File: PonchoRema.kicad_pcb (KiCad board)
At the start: 2 copper layers, 138.6 x 86.2 mm, 133 parts, among them J1 Conn_01x05, J10 Conn_01x05, J2 Conn_01x05, J3 Conn_01x05, J4 Conn_01x05, J5 Conn_01x05, J6 Conn_01x05, J7 Conn_01x03, J8 Conn_01x05, J9 Conn_01x05, P1 Conn_02x10_Odd_Even, SW1 SW_Push, SW2 SW_Push, U1 RPi-Pico, U10 ULN2004, U2 LTV-847S, U3 LTV-847S, U4 LTV-847S, U5 LTV-847S, U6 74HC14, U7 74HC14, U8 74HC14, U9 ULN2004

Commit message: Avances con el pcb antes de un laaargo finde
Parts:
- moved SW1 235.1 mm to (67.6, 103.6)
- moved U10 231.1 mm to (69.8, 128.2), turned to -90 degrees
- moved D22 225.1 mm to (55.9, 119.4)
- moved J9 220.4 mm to (74.9, 135.3), turned to -90 degrees
- moved R54 219.8 mm to (55.9, 115.6)
- moved D21 217.6 mm to (63.0, 119.4)
- moved R53 212.3 mm to (63.1, 115.6)
- moved D20 210.4 mm to (70.0, 119.4)
- moved R52 205.0 mm to (70.0, 115.6)
- moved D19 202.8 mm to (77.3, 119.4)
- moved D8 197.7 mm to (54.6, 86.6), turned to 180 degrees
- moved R51 197.5 mm to (77.3, 115.6)
- moved D7 190.3 mm to (61.3, 86.5), turned to 180 degrees
- moved D6 181.7 mm to (68.2, 86.5), turned to 180 degrees
- moved D18 175.0 mm to (132.7, 98.4), turned to 90 degrees
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
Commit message: Se agregan divisores resisitivos a la salida de los schmitt triggers para asegurar que no le lleguen 5V a las entradas de la pico. Se acutaliza el pcb y se acomodan los componentes en dos capas
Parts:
- added R61: 1k, Resistor_SMD:R_1206_3216Metric, B.Cu at (96.9, 80.6)
- added R62: 1k, Resistor_SMD:R_1206_3216Metric, B.Cu at (96.9, 86.6)
- added R63: 1k, Resistor_SMD:R_1206_3216Metric, B.Cu at (108.0, 80.6)
- added R64: 1k, Resistor_SMD:R_1206_3216Metric, B.Cu at (108.0, 86.6)
- added R65: 1k, Resistor_SMD:R_1206_3216Metric, B.Cu at (113.0, 80.6)
- added R66: 1k, Resistor_SMD:R_1206_3216Metric, B.Cu at (113.0, 86.4)
- added R67: 1k, Resistor_SMD:R_1206_3216Metric, B.Cu at (118.1, 80.6)
- added R68: 1k, Resistor_SMD:R_1206_3216Metric, B.Cu at (117.9, 86.4)
- added R69: 1k, Resistor_SMD:R_1206_3216Metric, B.Cu at (123.2, 80.9)
- added R70: 1k, Resistor_SMD:R_1206_3216Metric, B.Cu at (123.2, 86.6)
- added R71: 1k, Resistor_SMD:R_1206_3216Metric, B.Cu at (71.8, 80.6)
- added R72: 1k, Resistor_SMD:R_1206_3216Metric, B.Cu at (71.8, 86.4)
- added R73: 1k, Resistor_SMD:R_1206_3216Metric, B.Cu at (76.8, 80.6)
- added R74: 1k, Resistor_SMD:R_1206_3216Metric, B.Cu at (76.8, 86.4)
- added R75: 1k, Resistor_SMD:R_1206_3216Metric, B.Cu at (134.6, 81.1)
- added R76: 1k, Resistor_SMD:R_1206_3216Metric, B.Cu at (134.6, 86.6)
- added R77: 1k, Resistor_SMD:R_1206_3216Metric, B.Cu at (139.7, 80.9)
- added R78: 1k, Resistor_SMD:R_1206_3216Metric, B.Cu at (139.7, 87.0)
- added R79: 1k, Resistor_SMD:R_1206_3216Metric, B.Cu at (144.8, 81.3)
- added R80: 1k, Resistor_SMD:R_1206_3216Metric, B.Cu at (144.8, 87.0)
- added R81: 1k, Resistor_SMD:R_1206_3216Metric, B.Cu at (149.9, 81.3)
- added R82: 1k, Resistor_SMD:R_1206_3216Metric, B.Cu at (149.9, 87.0)
- added R83: 1k, Resistor_SMD:R_1206_3216Metric, B.Cu at (154.9, 80.9)
- added R84: 1k, Resistor_SMD:R_1206_3216Metric, B.Cu at (154.9, 87.0)
- added R85: 1k, Resistor_SMD:R_1206_3216Metric, B.Cu at (160.0, 81.3)
- added R86: 1k, Resistor_SMD:R_1206_3216Metric, B.Cu at (160.0, 87.0)
- added R87: 1k, Resistor_SMD:R_1206_3216Metric, B.Cu at (81.9, 80.6)
- added R88: 1k, Resistor_SMD:R_1206_3216Metric, B.Cu at (81.9, 86.4)
- added R89: 1k, Resistor_SMD:R_1206_3216Metric, B.Cu at (87.0, 80.6)
- added R90: 1k, Resistor_SMD:R_1206_3216Metric, B.Cu at (87.0, 86.4)
- added R91: 1k, Resistor_SMD:R_1206_3216Metric, B.Cu at (102.9, 80.6)
- added R92: 1k, Resistor_SMD:R_1206_3216Metric, B.Cu at (102.9, 86.4)
- C3, C4, C5, JP1, JP2, JP3, JP4, JP5, JP6, JP7, JP8, U10, U6, U7, U8, U9: moved to B.Cu
- U2, U3, U4, U5: footprint Package_DIP:SMDIP-16_W9.53mm -> Package_DIP:DIP-16_W7.62mm_Socket_LongPads
- moved R2 168.6 mm to (81.8, 96.2)
- moved D17 163.1 mm to (81.8, 100.3)
- moved C5 126.1 mm to (84.5, 64.1)
- moved JP5 116.5 mm to (104.8, 100.4), turned to 180 degrees
- moved C1 113.8 mm to (142.7, 128.7)
- moved C2 113.8 mm to (142.7, 132.1)
- moved JP7 111.5 mm to (115.6, 99.8), turned to 180 degrees
- moved JP6 110.0 mm to (109.8, 100.7), turned to 180 degrees
- moved JP8 104.2 mm to (121.5, 100.3), turned to 180 degrees
- moved JP1 104.0 mm to (104.8, 94.7), turned to 180 degrees
- moved TP5 103.8 mm to (126.4, 98.4)
- moved JP3 99.3 mm to (115.6, 94.7), turned to 180 degrees
- moved JP2 97.5 mm to (109.8, 95.0), turned to 180 degrees
- moved C3 93.3 mm to (117.3, 63.5)
- moved JP4 91.9 mm to (121.4, 94.7), turned to 180 degrees
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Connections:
- C3 pad 1: +3V3 -> +5V
- C4 pad 1: +3V3 -> +5V
- C5 pad 1: +3V3 -> +5V
- R10 pad 1: +3V3 -> +5V
- R12 pad 1: +3V3 -> +5V
- R13 pad 1: +3V3 -> +5V
- R15 pad 1: +3V3 -> +5V
- R16 pad 1: +3V3 -> +5V
- R18 pad 1: +3V3 -> +5V
- R19 pad 1: +3V3 -> +5V
- R21 pad 1: +3V3 -> +5V
- R22 pad 1: +3V3 -> +5V
- R24 pad 1: +3V3 -> +5V
- R25 pad 1: +3V3 -> +5V
- R27 pad 1: +3V3 -> +5V
- R28 pad 1: +3V3 -> +5V
- R3 pad 1: +3V3 -> +5V
- R30 pad 1: +3V3 -> +5V
- R31 pad 1: +3V3 -> +5V
- R33 pad 1: +3V3 -> +5V
- R34 pad 1: +3V3 -> +5V
- R36 pad 1: +3V3 -> +5V
- R37 pad 1: +3V3 -> +5V
- R39 pad 1: +3V3 -> +5V
- R4 pad 1: +3V3 -> +5V
- R40 pad 1: +3V3 -> +5V
- R42 pad 1: +3V3 -> +5V
- R43 pad 1: +3V3 -> +5V
- R45 pad 1: +3V3 -> +5V
- R46 pad 1: +3V3 -> +5V
- R48 pad 1: +3V3 -> +5V
- R49 pad 1: +3V3 -> +5V
- R6 pad 1: +3V3 -> +5V
- R7 pad 1: +3V3 -> +5V
- R9 pad 1: +3V3 -> +5V
- U6 pad 10: /inputs/DIN12 -> Net-(R67-Pad2)
- U6 pad 12: /inputs/DIN13 -> Net-(R69-Pad2)
- U6 pad 14: +3V3 -> +5V
- U6 pad 2: /inputs/DIN8 -> Net-(R61-Pad2)
- U6 pad 4: /inputs/DIN9 -> Net-(R91-Pad2)
- U6 pad 6: /inputs/DIN10 -> Net-(R63-Pad2)
- U6 pad 8: /inputs/DIN11 -> Net-(R65-Pad2)
- U7 pad 10: /inputs/DIN4 -> Net-(R83-Pad2)
- U7 pad 12: /inputs/DIN5 -> Net-(R85-Pad2)
- U7 pad 14: +3V3 -> +5V
- U7 pad 2: /inputs/DIN0 -> Net-(R75-Pad2)
- U7 pad 4: /inputs/DIN1 -> Net-(R77-Pad2)
- U7 pad 6: /inputs/DIN2 -> Net-(R79-Pad2)
- U7 pad 8: /inputs/DIN3 -> Net-(R81-Pad2)
- U8 pad 14: +3V3 -> +5V
- U8 pad 2: /inputs/DIN14 -> Net-(R71-Pad2)
- U8 pad 4: /inputs/DIN15 -> Net-(R73-Pad2)
- U8 pad 6: /inputs/DIN6 -> Net-(R87-Pad2)
- U8 pad 8: /inputs/DIN7 -> Net-(R89-Pad2)

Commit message: Comienza ruteo en pcb
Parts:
- D17: value LedRed -> SPI_ERR
- J1: value Conn_01x05 -> IN_X
- J10: value Conn_01x05 -> DOUT_5-9
- J2: value Conn_01x05 -> IN_Y
- J3: value Conn_01x05 -> IN_Z
- J4: value Conn_01x05 -> IN_W
- J5: value Conn_01x05 -> X_Y_LIMITS
- J6: value Conn_01x05 -> Z_W_LIMITS
- J7: value Conn_01x03 -> 1W
- J9: value Conn_01x05 -> DOUT_0-4
- R12, R15, R18, R21, R24, R27, R3, R30, R33, R36, R39, R42, R45, R48, R6, R9: value 560 -> 330
- R61, R63, R65, R67, R69, R71, R73, R75, R77, R79, R81, R83, R85, R87, R89, R91: value 1k -> 100k
- R62, R64, R66, R68, R70, R72, R74, R76, R78, R80, R82, R84, R86, R88, R90: value 1k -> 220k
- SW1: value SW_Push -> PICO-RST; footprint Button_Switch_SMD:SW_Push_1P1T_NO_CK_KSC7xxJ -> Button_Switch_THT:SW_PUSH_6mm
- SW2: footprint Button_Switch_SMD:SW_Push_1P1T_NO_CK_KSC7xxJ -> Button_Switch_THT:SW_PUSH_6mm
- moved J8 131.5 mm to (53.3, 95.2)
- moved R55 63.2 mm to (80.6, 121.8)
- moved D24 63.1 mm to (80.6, 125.3)
- moved R2 43.2 mm to (101.5, 134.6), turned to 180 degrees
- moved D17 42.7 mm to (107.3, 134.6), turned to 180 degrees
- moved TP0 41.3 mm to (157.5, 107.3)
- moved JP1 39.5 mm to (95.0, 133.0), turned to -90 degrees
- moved JP7 37.3 mm to (151.8, 109.0), turned to -90 degrees
- moved JP3 34.2 mm to (146.7, 109.0), turned to -90 degrees
- moved JP5 32.8 mm to (100.6, 133.0), turned to -90 degrees
- moved R85 31.3 mm to (128.9, 84.6)
- moved R86 31.3 mm to (128.9, 90.3)
- moved TP3 26.6 mm to (143.6, 124.5)
- moved R69 26.3 mm to (97.1, 84.6)
- moved R70 26.3 mm to (97.2, 90.3)
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- renumbered D9 to D0, D10 to D1, D3 to D10, D4 to D11, D5 to D12, D6 to D13, D7 to D14, D8 to D15, D11 to D2, D19 to D20, D20 to D21, D21 to D22, D22 to D23, D23 to D24, D24 to D25, D25 to D26, D26 to D27, D27 to D28, D28 to D29, D12 to D3, D13 to D4, D14 to D5, D15 to D6, D16 to D7, D1 to D8, D2 to D9
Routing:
- net +5V: track 0.00 -> 245.7 mm
- net /inputs/COM: track 0.00 -> 195.6 mm
- net Net-(D12-K): track 0.00 -> 30.4 mm
- net Net-(D13-K): track 0.00 -> 26.5 mm
- net Net-(D14-K): track 0.00 -> 24.9 mm
- net Net-(D11-K): track 0.00 -> 23.9 mm
- net Net-(D15-K): track 0.00 -> 23.6 mm
- net Net-(D10-K): track 0.00 -> 23.2 mm
- net Net-(J3-Pin_2): track 0.00 -> 16.8 mm
- net Net-(J3-Pin_5): track 0.00 -> 14.8 mm
- net Net-(J1-Pin_2): track 0.00 -> 14.5 mm
- net Net-(D3-K): track 0.00 -> 14.1 mm
- net Net-(J1-Pin_5): track 0.00 -> 12.6 mm
- net Net-(J4-Pin_2): track 0.00 -> 12.6 mm
- net Net-(D2-K): track 0.00 -> 12.5 mm
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
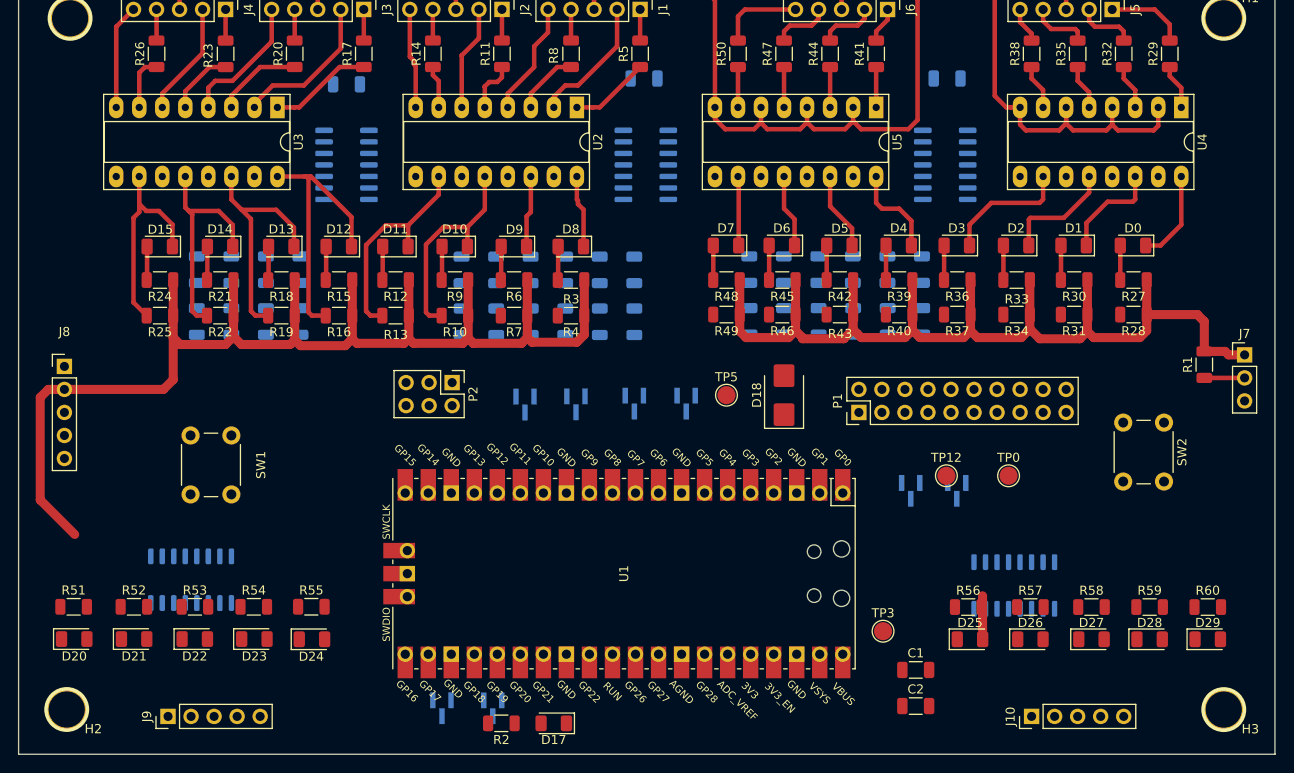
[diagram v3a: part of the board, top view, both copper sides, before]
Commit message: capa top lista, falta capa bottom del pcb
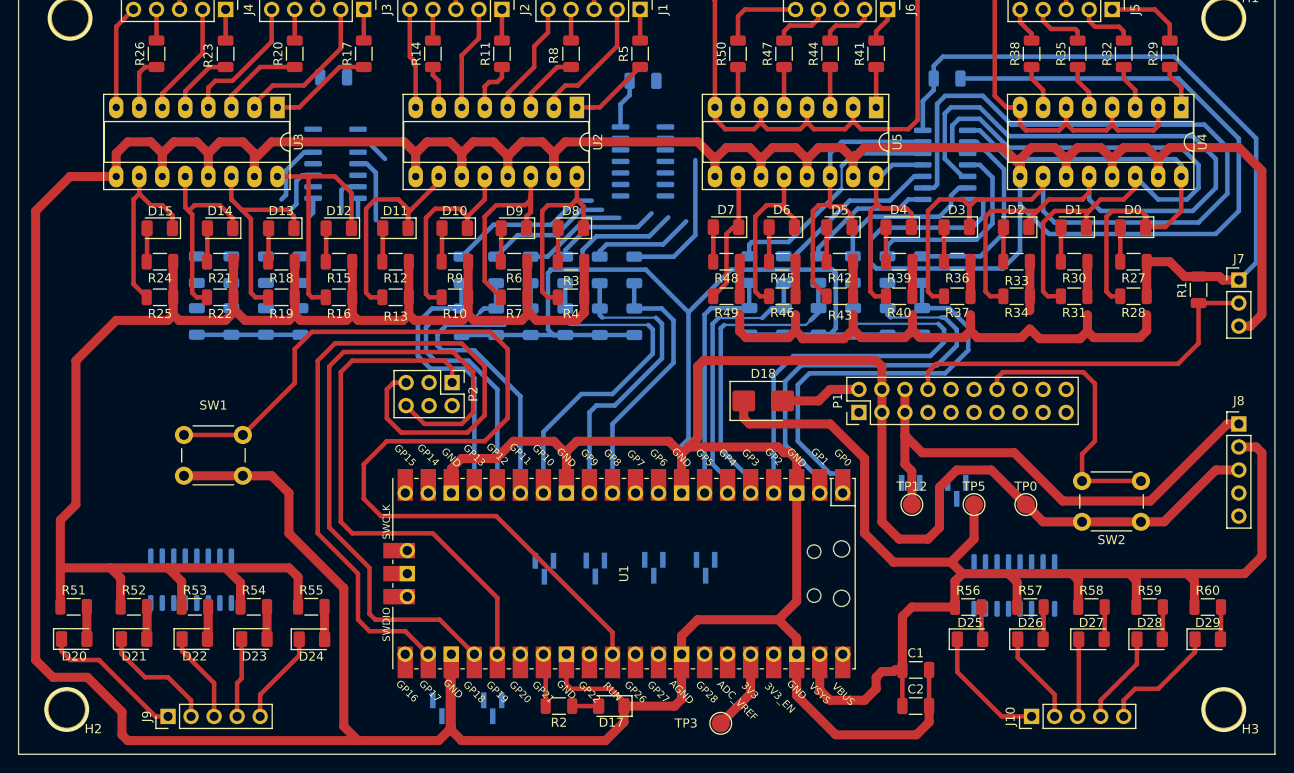
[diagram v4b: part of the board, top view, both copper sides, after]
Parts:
- moved J8 129.7 mm to (182.9, 101.6)
- moved C3 34.2 mm to (83.0, 63.4)
- moved U6 34.2 mm to (83.2, 72.9)
- moved C5 32.7 mm to (117.2, 63.8)
- moved U8 32.7 mm to (117.2, 72.6)
- moved TP5 29.9 mm to (153.7, 110.5)
- moved TP3 20.6 mm to (125.7, 134.6)
- moved JP2 18.2 mm to (118.3, 117.5)
- moved JP4 18.2 mm to (106.3, 117.6)
- moved JP6 18.2 mm to (124.1, 117.5)
- moved JP8 18.2 mm to (111.9, 117.5)
- moved SW2 11.2 mm to (172.1, 112.4), turned to 180 degrees
- moved J7 8.28 mm to (182.9, 85.7)
- moved R1 8.28 mm to (178.4, 86.8)
- moved D17 6.63 mm to (113.7, 132.7)
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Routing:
- net GND: track 0.00 -> 889.3 mm
- net +5V: track 245.7 -> 500.5 mm
- net Net-(U1-RUN): track 0.00 -> 108.8 mm
- net Net-(D3-K): track 14.1 -> 107.3 mm
- net /uC/SPI_CS: track 0.00 -> 83.2 mm
- net Net-(D2-K): track 12.5 -> 89.1 mm
- net /uC/SPI_SCK: track 0.00 -> 73.2 mm
- net /uC/SPI_MISO: track 0.00 -> 58.2 mm
- net Net-(D1-K): track 11.5 -> 69.0 mm
- net +12V: track 0.00 -> 56.4 mm
- net /inputs/DIN2: track 0.00 -> 49.3 mm
- net /inputs/DIN1: track 0.00 -> 48.0 mm
- net /inputs/DIN0: track 0.00 -> 46.1 mm
- net Net-(D0-K): track 10.2 -> 51.0 mm
- net /inputs/DIN10: track 0.00 -> 39.1 mm
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
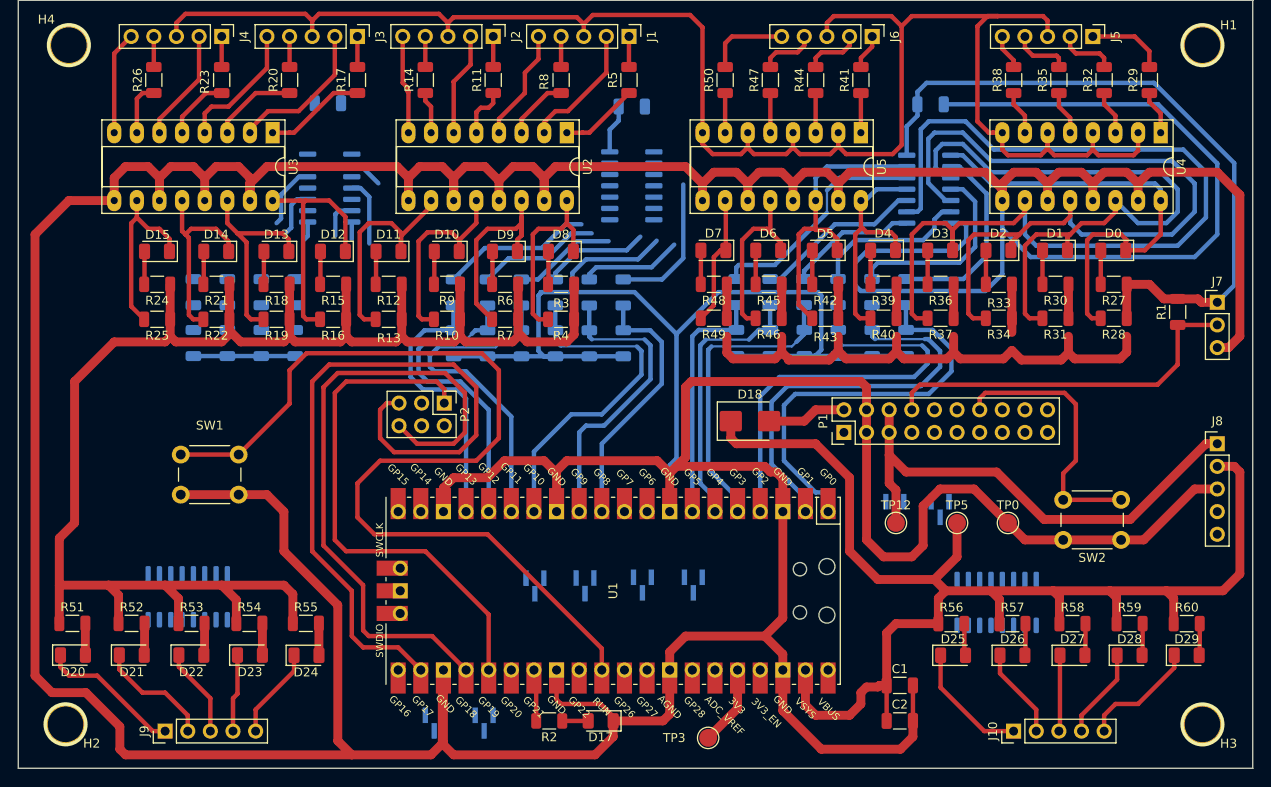
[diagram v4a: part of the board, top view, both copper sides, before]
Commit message: PCB: Faltan rutear 4 líneas de la capa bottom
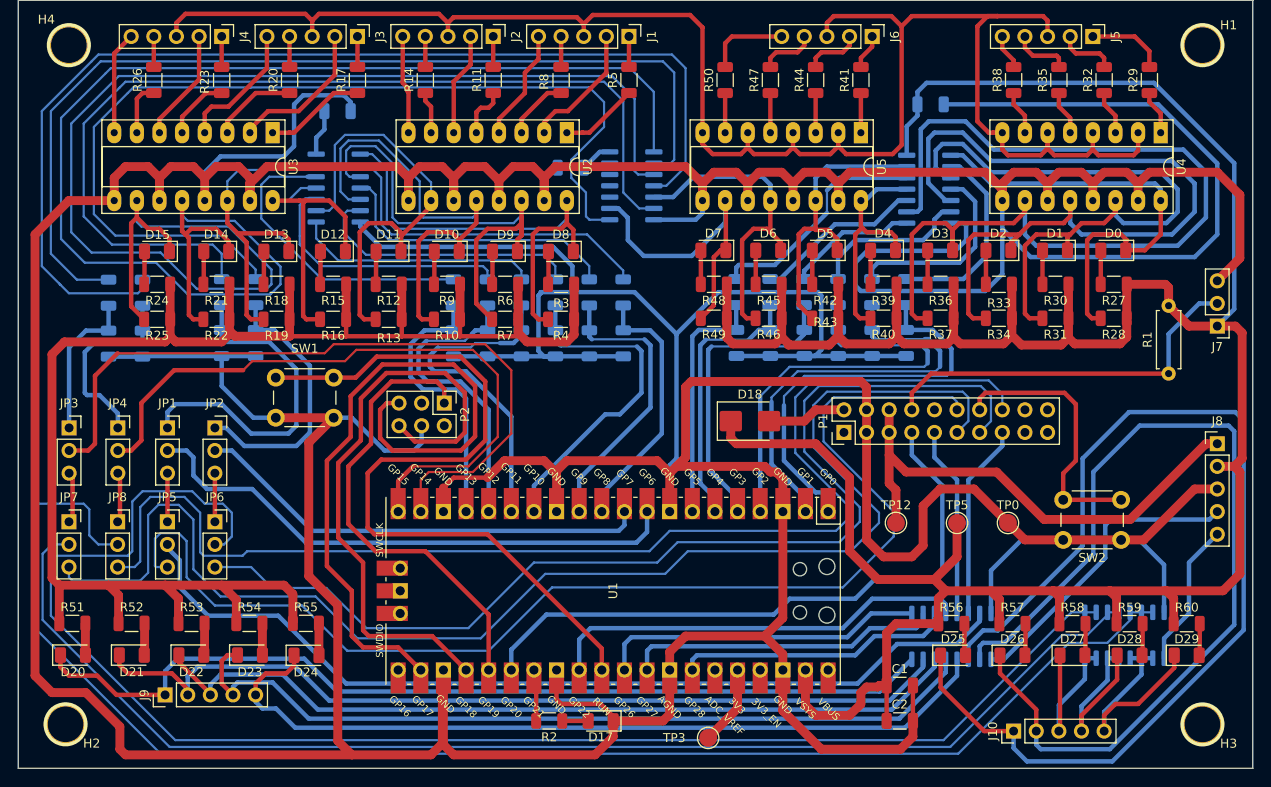
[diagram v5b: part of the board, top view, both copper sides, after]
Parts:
- JP1, JP2, JP3, JP4, JP5, JP6, JP7, JP8: footprint Connector_PinHeader_1.00mm:PinHeader_1x03_P1.00mm_Vertical_SMD_Pin1Left -> Connector_PinSocket_2.54mm:PinSocket_1x03_P2.54mm_Vertical; moved to F.Cu
- R1: footprint Resistor_SMD:R_1206_3216Metric -> Resistor_THT:R_Axial_DIN0207_L6.3mm_D2.5mm_P7.62mm_Horizontal
- moved JP7 97.8 mm to (54.0, 110.4), turned to 0 degrees
- moved JP3 93.1 mm to (54.0, 99.8), turned to 0 degrees
- moved U10 85.8 mm to (153.0, 123.2)
- moved JP6 54.2 mm to (70.4, 110.4), turned to 0 degrees
- moved JP8 53.0 mm to (59.4, 110.4), turned to 0 degrees
- moved JP2 51.1 mm to (70.4, 99.8), turned to 0 degrees
- moved JP4 50.1 mm to (59.5, 99.8), turned to 0 degrees
- moved JP1 44.7 mm to (65.0, 99.8), turned to 0 degrees
- moved JP5 42.1 mm to (65.0, 110.4), turned to 0 degrees
- moved U9 14.8 mm to (172.5, 123.1)
- moved SW1 13.7 mm to (77.2, 94.2)
- moved C5 9.69 mm to (110.3, 70.6), turned to 180 degrees
- moved R73 9.53 mm to (62.2, 84.6)
- moved R74 9.53 mm to (62.2, 90.4)
- moved R71 9.53 mm to (58.4, 84.6)
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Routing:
- net /outputs/DOUT7: track 0.00 -> 168.2 mm
- net /outputs/DOUT9: track 0.00 -> 165.0 mm
- net /uC/CIAA_GPIO4: track 0.00 -> 153.4 mm
- net /outputs/DOUT8: track 0.00 -> 144.0 mm
- net /uC/CIAA_GPIO9: track 0.00 -> 138.5 mm
- net Net-(D15-K): track 20.2 -> 156.1 mm
- net /uC/CIAA_GPIO5: track 0.00 -> 135.2 mm
- net Net-(D14-K): track 21.4 -> 156.5 mm
- net /uC/CIAA_GPIO6: track 0.00 -> 123.0 mm
- net Net-(R73-Pad2): track 0.00 -> 122.4 mm
- net Net-(R89-Pad2): track 0.00 -> 109.5 mm
- net Net-(R71-Pad2): track 0.00 -> 108.7 mm
- net Net-(R87-Pad2): track 0.00 -> 108.4 mm
- net /outputs/Spare5: track 13.8 -> 121.3 mm
- net GND: track 889.3 -> 994.3 mm
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
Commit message: pcb listo, ver detalles
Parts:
- JP1, JP2, JP3, JP4, JP5, JP6, JP7, JP8: footprint Connector_PinSocket_2.54mm:PinSocket_1x03_P2.54mm_Vertical -> Connector_PinHeader_2.54mm:PinHeader_1x03_P2.54mm_Vertical
- U2, U3, U4, U5: footprint Package_DIP:DIP-16_W7.62mm_Socket_LongPads -> Package_DIP:DIP-16_W7.62mm_LongPads
- moved R2 0.25 mm to (107.6, 132.7)
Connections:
- H1 pad 1: (no net) -> GND
- H2 pad 1: (no net) -> GND
- H3 pad 1: (no net) -> GND
- H4 pad 1: (no net) -> GND
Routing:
- net +5V: track 527.8 -> 641.9 mm
- net GND: track 994.3 -> 1103.1 mm
- net /uC/SPI_MOSI: track 0.27 -> 45.6 mm, vias 0 -> 2
- net /uC/CIAA_GPIO6: track 123.0 -> 133.1 mm
- net /uC/CIAA_GPIO4: track 153.4 -> 163.2 mm
- net /uC/CIAA_GPIO5: track 135.2 -> 143.8 mm
- net /uC/IRQ_TO_REMA: track 71.5 -> 64.1 mm
- net Net-(R73-Pad2): track 122.4 -> 129.6 mm
- net Net-(R71-Pad2): track 108.7 -> 115.6 mm
- net /uC/CIAA_GPIO9: track 138.5 -> 144.2 mm
- net Net-(D14-K): track 156.5 -> 159.3 mm
- net Net-(U1-RUN): track 87.4 -> 89.7 mm
- net Net-(J3-Pin_2): track 16.8 -> 19.1 mm
- net Net-(JP4-C): track 77.1 -> 75.1 mm
- net Net-(D15-K): track 156.1 -> 157.9 mm
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- added copper zone on B.Cu, net GND
- added copper zone on F.Cu, net GND
